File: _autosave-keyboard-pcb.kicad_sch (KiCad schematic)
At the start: 21 parts, among them J1 AVR-ISP-6, SW1 SW_Push, U1 ATmega32U4-A, U2 PRTR5V0U2X, Y1 16MHz

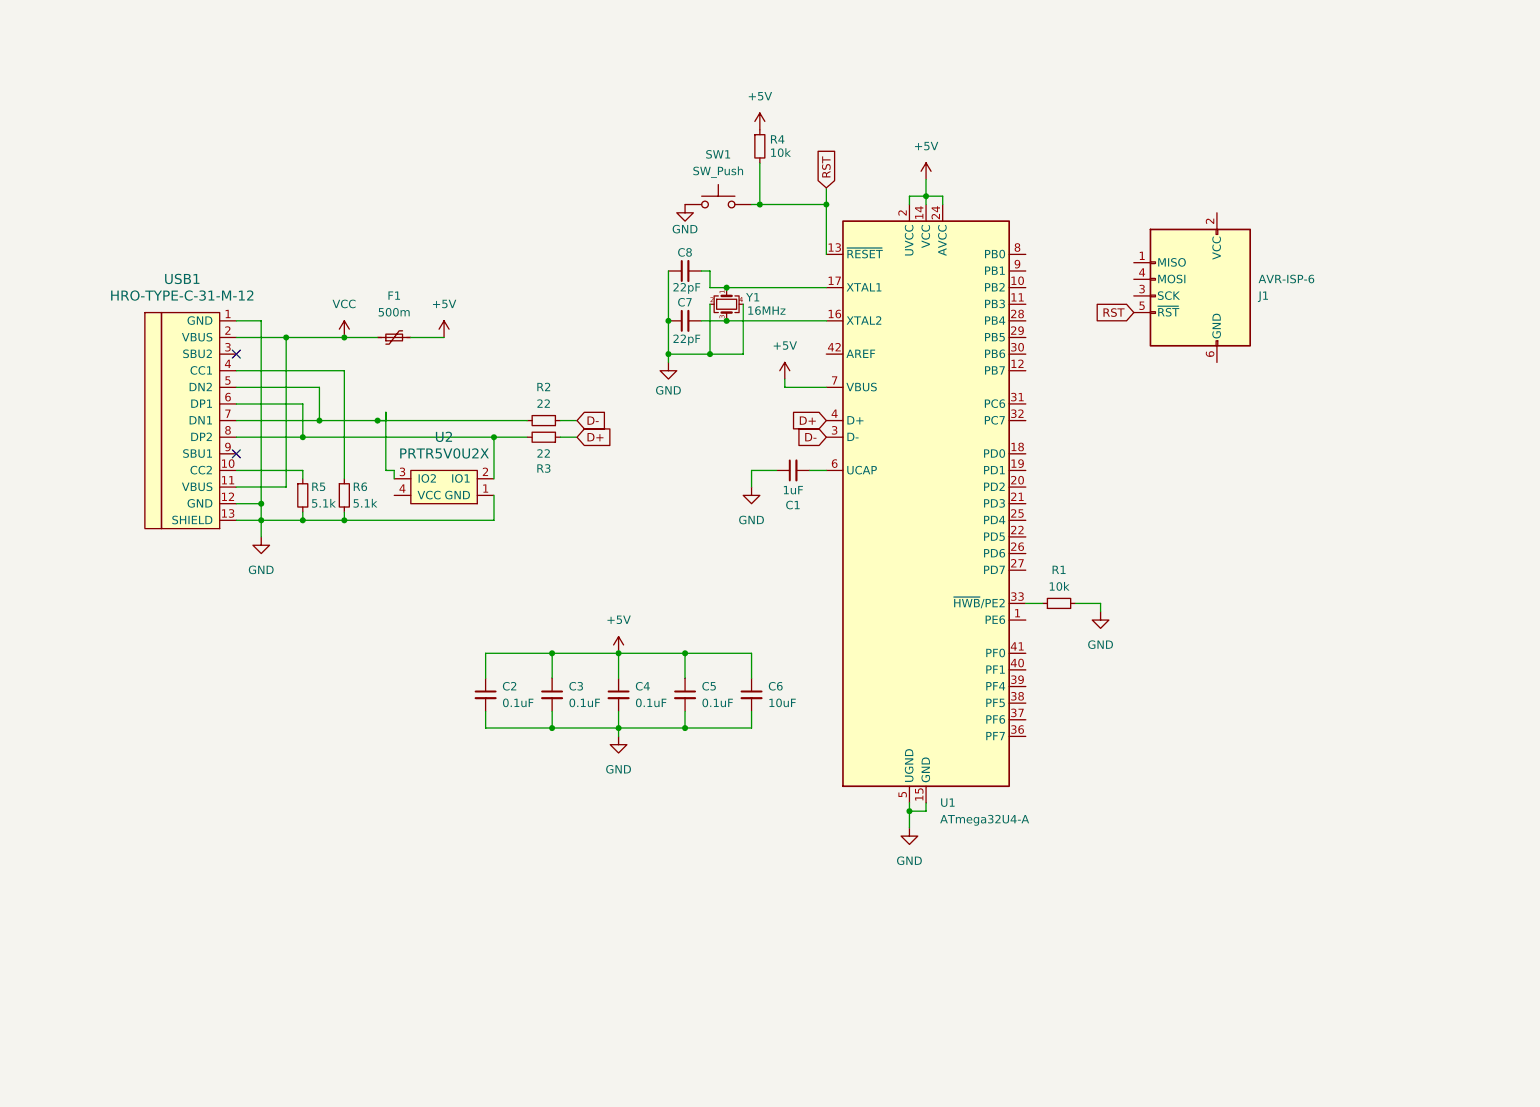
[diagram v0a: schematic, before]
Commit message: Constructed TKL keyswitch matrix
An 87 MX switch matrix with diodes
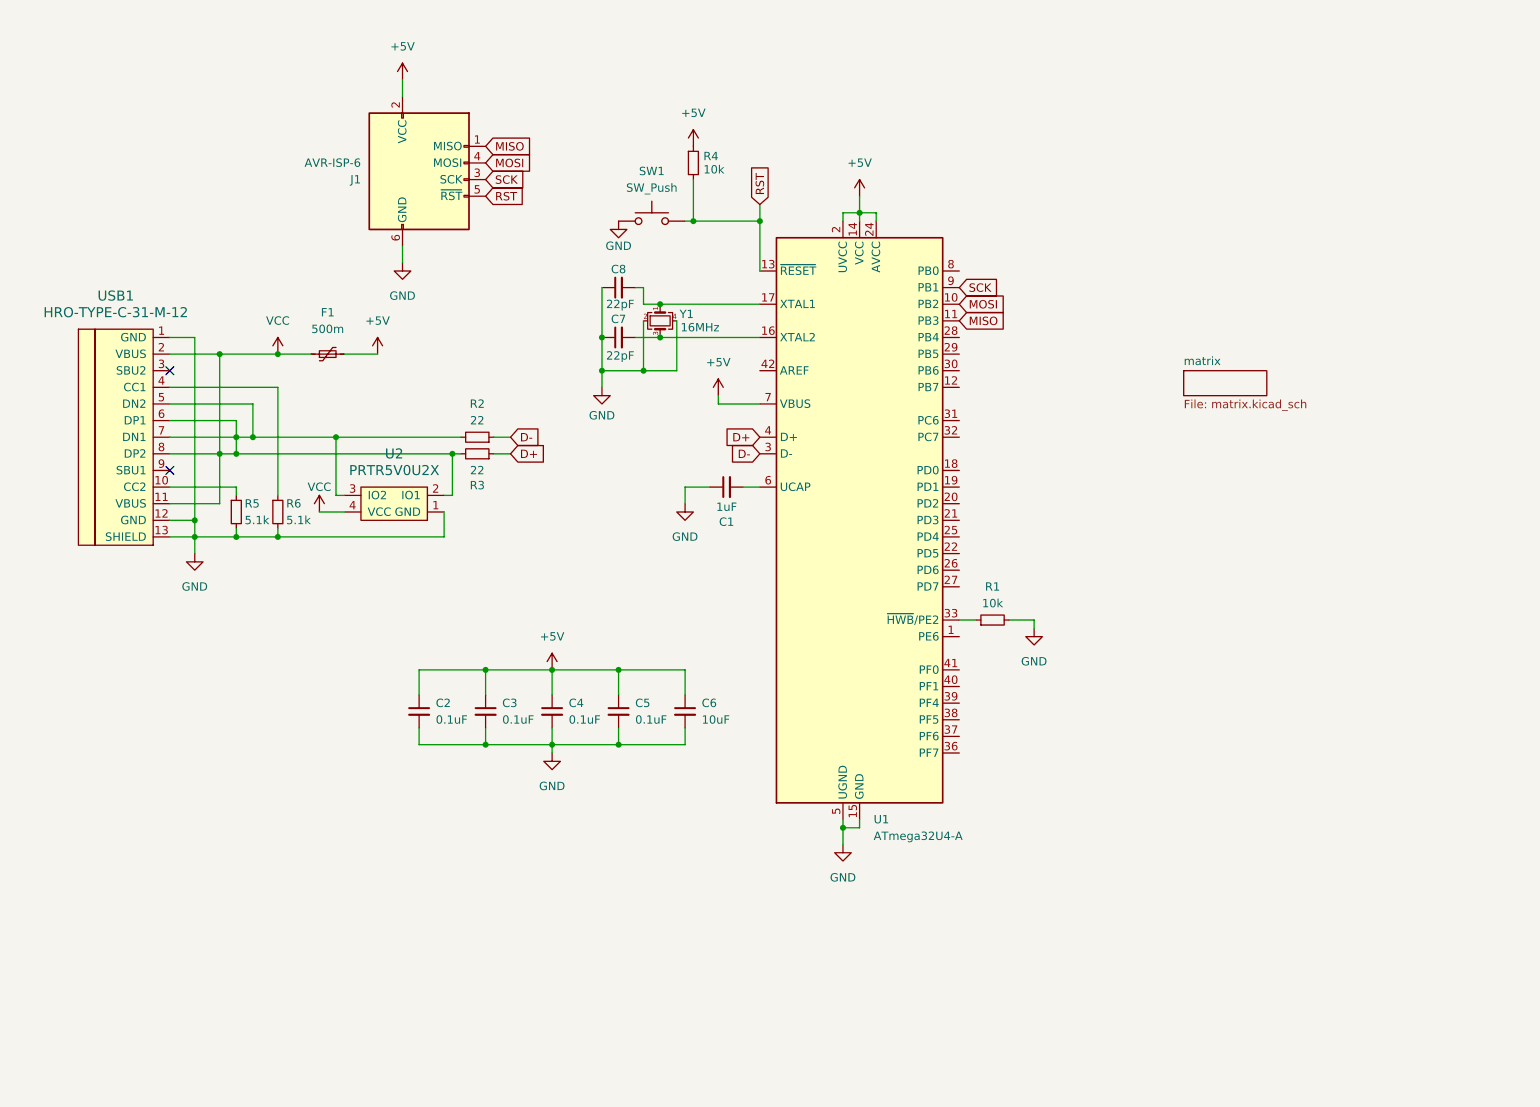
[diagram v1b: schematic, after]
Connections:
- net +5V: now also J1.2 (VCC)
- net GND: now also J1.6 (GND)
- net VCC: now also R2.2, R3.2, U2.2 (IO1), U2.3 (IO2), U2.4 (VCC), USB1.5 (DN2), USB1.6 (DP1), USB1.7 (DN1), USB1.8 (DP2)
- net MISO: now reaches J1.1 (MISO)
- net MISO: now also U1.11 (PB3)
- net SCK: now reaches J1.3 (SCK)
- net SCK: now also U1.9 (PB1)
- net MOSI: now reaches J1.4 (MOSI)
- net MOSI: now also U1.10 (PB2)
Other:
- added sheet matrix (matrix.kicad_sch)
- moved on the sheet: C1, C2, C3, C4, C5, C6, C7, C8, F1, J1, R1, R2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

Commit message: Changed MCU circuitry
Atmega32u4 -> rp2040, updated USB-C connector, updated ESD protection, added memory chip, added voltage regulator
Tutorial followed: https://youtu.be/6Z49bynRqj8?si=SZUICHd2tr064eZg
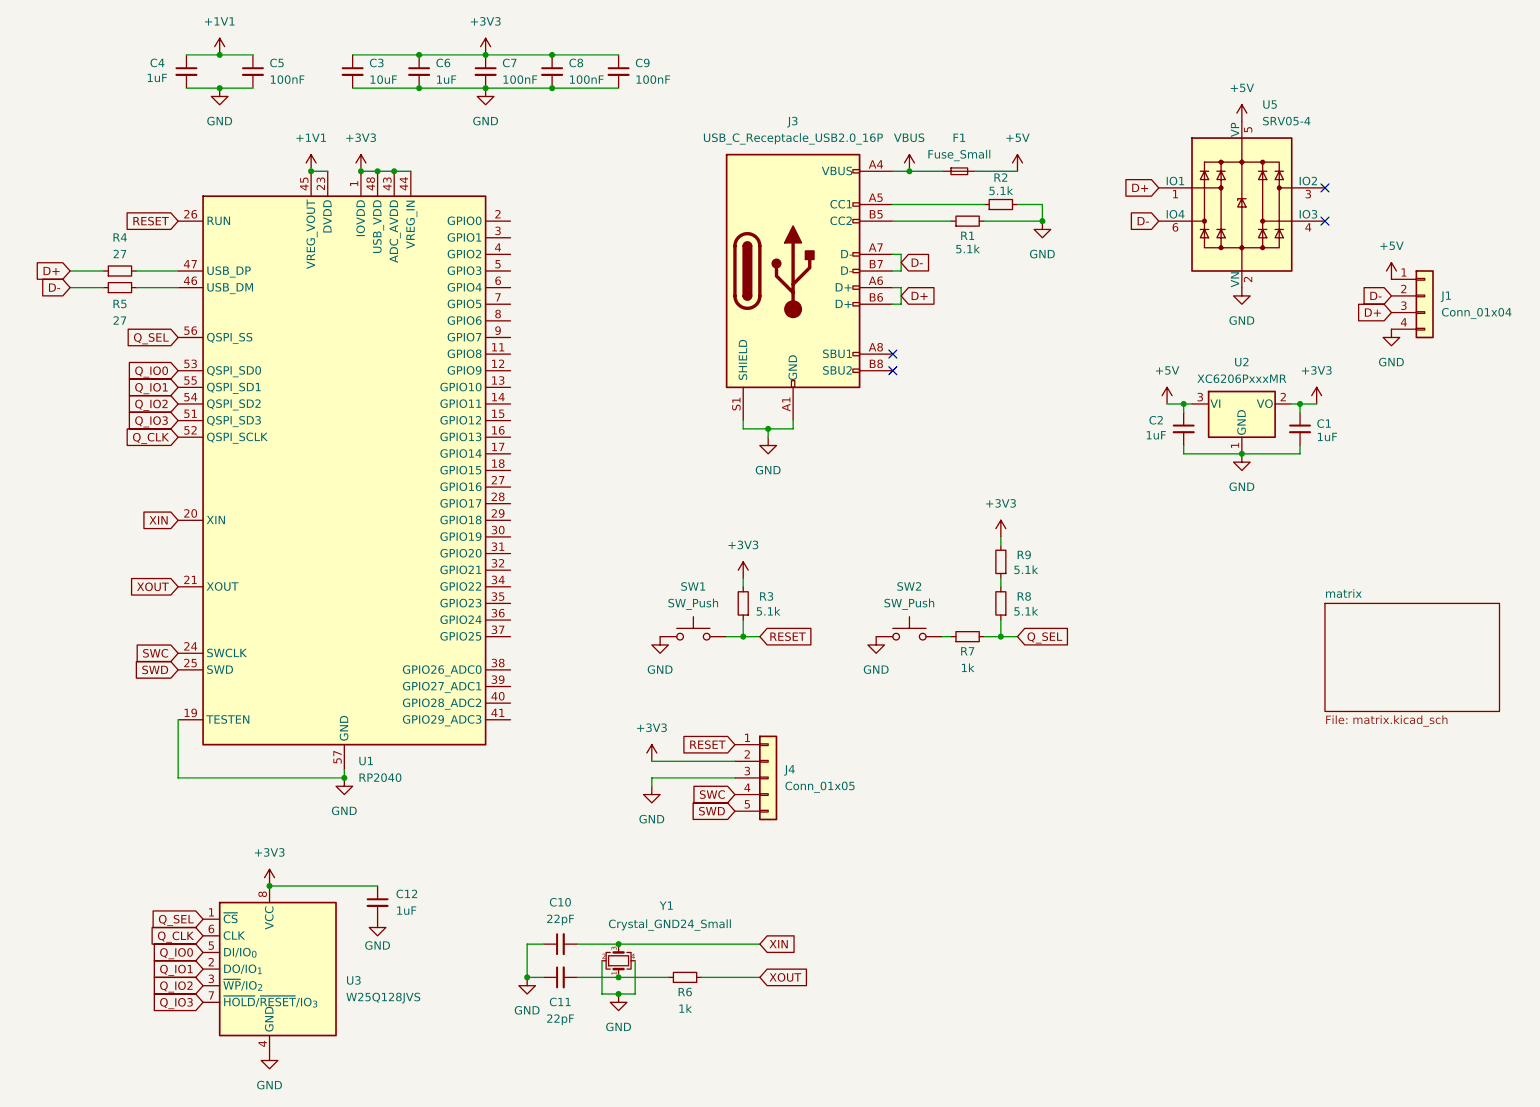
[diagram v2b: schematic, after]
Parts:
- removed F1: 500m, symbol Device:Polyfuse_Small
- removed J1: AVR-ISP-6, symbol Connector:AVR-ISP-6
- removed U1: ATmega32U4-A, Package_QFP:TQFP-44_10x10mm_P0.8mm, symbol MCU_Microchip_ATmega:ATmega32U4-A
- removed U2: PRTR5V0U2X, symbol random-keyboard-parts:PRTR5V0U2X
- removed USB1: HRO-TYPE-C-31-M-12, symbol Type-C:HRO-TYPE-C-31-M-12
- added C10, C11: 22pF, symbol Device:C_Small
- added C12: 1uF, symbol Device:C_Small
- added C9: 100nF, symbol Device:C_Small
- added F1: Fuse_Small, symbol Device:Fuse_Small
- added J1: Conn_01x04, symbol Connector_Generic:Conn_01x04
- added J3: USB_C_Receptacle_USB2.0_16P, symbol Connector:USB_C_Receptacle_USB2.0_16P
- added J4: Conn_01x05, symbol Connector_Generic:Conn_01x05
- added R7: 1k, symbol Device:R_Small
- added R8, R9: 5.1k, symbol Device:R_Small
- added SW2: SW_Push, symbol Switch:SW_Push
- added U1: RP2040, Package_DFN_QFN:QFN-56-1EP_7x7mm_P0.4mm_EP3.2x3.2mm, symbol MCU_RaspberryPi:RP2040
- added U2: XC6206PxxxMR, Package_TO_SOT_SMD:SOT-23-3, symbol Regulator_Linear:XC6206PxxxMR
- added U3: W25Q128JVS, Package_SO:SOIC-8_5.3x5.3mm_P1.27mm, symbol Memory_Flash:W25Q128JVS
- added U5: SRV05-4, PCM_marbastlib-various:SOT-23-6-routable, symbol PCM_marbastlib-various:SRV05-4
- C2, C4: value 0.1uF -> 1uF
- C3: value 0.1uF -> 10uF
- C5: value 0.1uF -> 100nF
- C6: value 10uF -> 1uF
- C7, C8: value 22pF -> 100nF
- R1: value 10k -> 5.1k
- R2, R3: value 22 -> 5.1k
- R4: value 10k -> 27
- R5: value 5.1k -> 27
- R6: value 5.1k -> 1k
- Y1: value 16MHz -> Crystal_GND24_Small
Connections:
- net +5V: now also F1.2, J1.1 (Pin_1), U2.3 (VI), U5.5 (VP); no longer C3.1, C4.1, C5.1, C6.1, R4.1
- net D+: now also R4.1, J1.3 (Pin_3), J3.A6 (D+), J3.B6 (D+), U5.1 (IO1); no longer R3.1
- net D-: now also R5.1, J1.2 (Pin_2), J3.A7 (D-), J3.B7 (D-), U5.6 (IO4); no longer R2.1
- net GND: now also C1.2, C7.2, C8.2, R2.2, C10.1, C11.1, C12.2, C9.2, J1.4 (Pin_4), J3.A1 (GND), J3.A12 (GND), J3.B1 (GND), J3.B12 (GND), J3.S1 (SHIELD), J4.3 (Pin_3), SW2.1, U1.19 (TESTEN), U1.57 (GND), U2.1 (GND), U3.4 (GND), U5.2 (VN); no longer C1.1, C7.1, C8.1, R5.2, R6.2
- net at R6.1: now also Y1.1, C11.2
- net XIN: now reaches Y1.3
- net XIN: now also C10.2, U1.20 (XIN); no longer C7.2
- net at R1.1: now also J3.B5 (CC2)
- net RST: no longer names the net of R4.2
- net RST: now also U1.47 (USB_DP); no longer SW1.2
- net VCC renamed +3V3
- net +3V3: now also C1.1, C3.1, C6.1, C7.1, C8.1, C12.1, C9.1, J4.2 (Pin_2), R9.2, U1.1 (IOVDD), U1.10 (IOVDD), U1.22 (IOVDD), U1.33 (IOVDD), U1.42 (IOVDD), U1.43 (ADC_AVDD), U1.44 (VREG_IN), U1.48 (USB_VDD), U1.49 (IOVDD), U2.2 (VO), U3.8 (VCC); no longer R2.2
- new net: R7.1, SW2.2
- new net: R5.2, U1.46 (USB_DM)
- new net: J3.A5 (CC1), R2.1
- new net: R8.2, R9.1
- new net +1V1: C4.1, C5.1, U1.23 (DVDD), U1.45 (VREG_VOUT), U1.50 (DVDD)
- new net Q_CLK: U1.52 (QSPI_SCLK), U3.6 (CLK)
- new net Q_IO0: U1.53 (QSPI_SD0), U3.5 (DI/IO_{0})
- new net Q_IO1: U1.55 (QSPI_SD1), U3.2 (DO/IO_{1})
- new net Q_IO2: U1.54 (QSPI_SD2), U3.3 (~{WP}/IO_{2})
- new net Q_IO3: U1.51 (QSPI_SD3), U3.7 (~{HOLD}/~{RESET}/IO_{3})
- new net Q_SEL: R7.2, R8.1, U1.56 (QSPI_SS), U3.1 (~{CS})
- new net RESET: J4.1 (Pin_1), R3.1, SW1.2, U1.26 (RUN)
- new net SWC: J4.4 (Pin_4), U1.24 (SWCLK)
- new net SWD: J4.5 (Pin_5), U1.25 (SWD)
- new net VBUS: F1.1, J3.A4 (VBUS), J3.A9 (VBUS), J3.B4 (VBUS), J3.B9 (VBUS)
- new net XOUT: R6.2, U1.21 (XOUT)
- no-connect marks 2 -> 4
